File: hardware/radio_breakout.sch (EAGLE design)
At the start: 14 parts

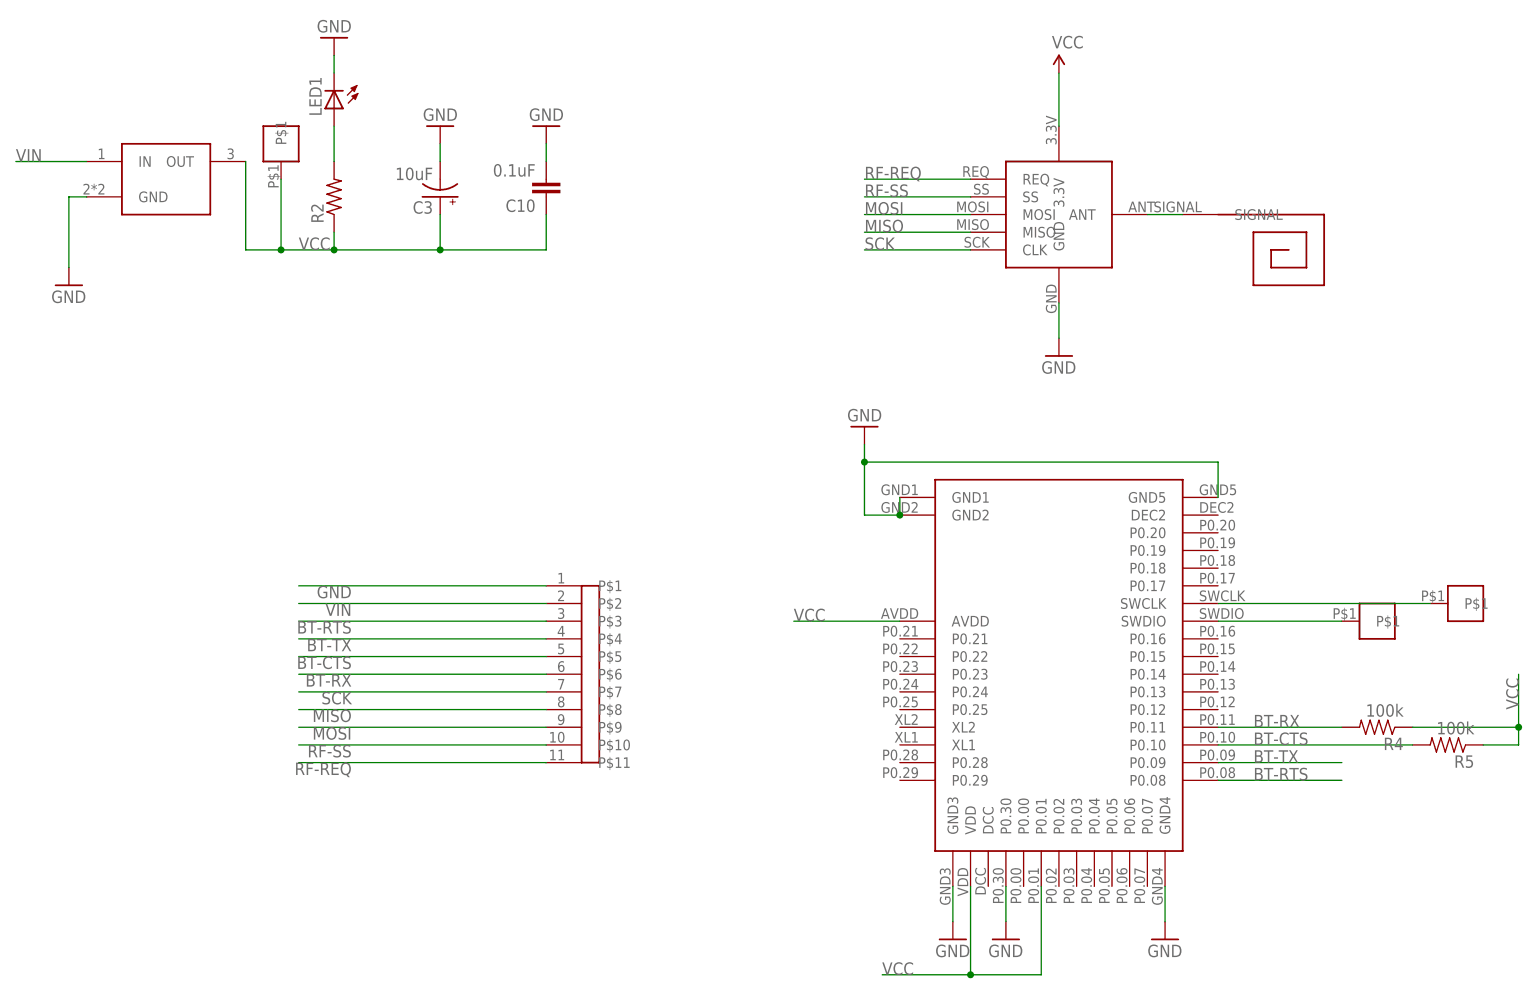
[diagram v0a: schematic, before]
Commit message: replaced UART with SPI bluefruit software and hardware
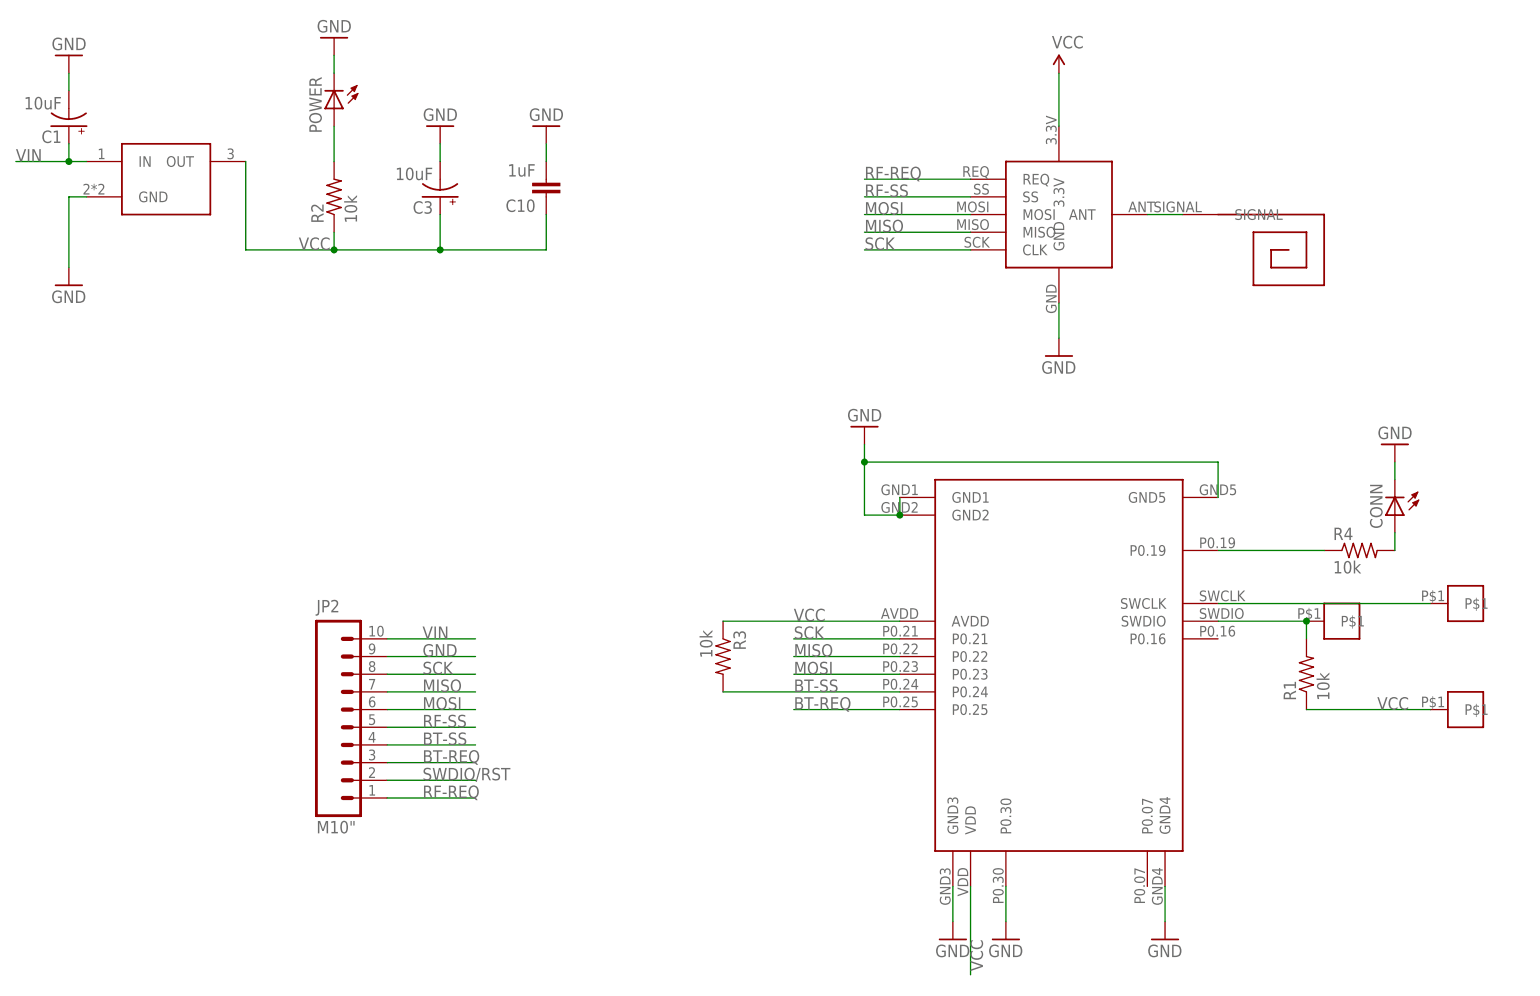
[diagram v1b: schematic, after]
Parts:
- removed DATA: PAD, ITP_Lab:PAD
- removed R5: 100k, SparkFun-Resistors:RESISTOR0603
- removed U$4: MDBT40, ITP_Lab:MDBT40
- added C1: 10uF, SparkFun-Capacitors:CAP_POL1206
- added CLOCK1: PAD, ITP_Lab:PAD
- added CONN: (no value), adafruit:LEDCHIP-LED0603
- added JP2: M10", SparkFun-Connectors:M10"
- added R1, R3: 10k, SparkFun-Resistors:RESISTOR0603
- C10: value 0.1uF -> 1uF
- R2: value (none) -> 10k
- R4: value 100k -> 10k; device SparkFun-Resistors:RESISTOR0603 -> adafruit:R-US_R0603
- U$5: value HEADER-11 -> NRF51-MDBT40-SPI; device ITP_Lab:HEADER-11 -> ITP_Lab:NRF51-MDBT40-SPI
- renumbered LED1 to POWER
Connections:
- removed net BT-CTS: R5.2, U$4.P0.10, U$5.P$5
- removed net BT-RTS: U$4.P0.08, U$5.P$3
- removed net BT-RX: R4.2, U$4.P0.11, U$5.P$6
- removed net BT-TX: U$4.P0.09, U$5.P$4
- removed net N$12: DATA.P$1, U$4.SWDIO
- new net BT-REQ: JP2.3, U$5.P0.25
- new net BT-SS: JP2.4, R3.2, U$5.P0.24
- new net N$2: R4.1, U$5.P0.19
- new net N$4: CONN.A, R4.2
- new net SWDIO/RST: CLOCK1.P$1, JP2.2, R1.2, U$5.SWDIO
- net GND: now also C1.-, CONN.C, JP2.9, U$5.GND1, U$5.GND2, U$5.GND3, U$5.GND4, U$5.GND5, U$5.P0.30; no longer U$4.GND1, U$4.GND2, U$4.GND3, U$4.GND4, U$4.GND5, U$4.P0.30, U$5.P$1
- net MISO: now also JP2.7, U$5.P0.22; no longer U$5.P$8
- net MOSI: now also JP2.6, U$5.P0.23; no longer U$5.P$9
- net N$11: now also U$5.SWCLK; no longer U$4.SWCLK
- net RF-REQ: now also JP2.1; no longer U$5.P$11
- net RF-SS: now also JP2.5; no longer U$5.P$10
- net SCK: now also JP2.8, U$5.P0.21; no longer U$5.P$7
- net VCC: now also R1.1, R3.1, U$5.AVDD, U$5.VDD; no longer R4.1, R5.1, U$4.AVDD, U$4.P0.01, U$4.VDD
- net VIN: now also C1.+, JP2.10; no longer U$5.P$2
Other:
- moved on the sheet: R4
